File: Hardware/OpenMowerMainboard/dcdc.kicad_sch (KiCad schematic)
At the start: 24 parts, among them IC3 MAX20405AFOF_VY+T, U1 LM2596S_MODULE

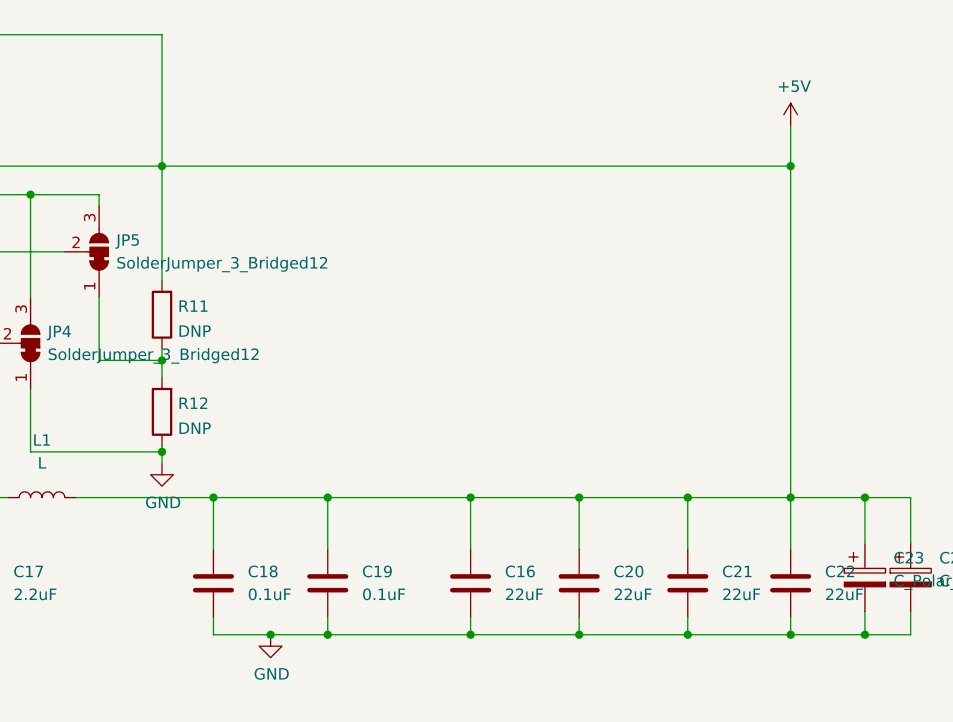
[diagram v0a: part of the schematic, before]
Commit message: v0_9_1 mainboard rework
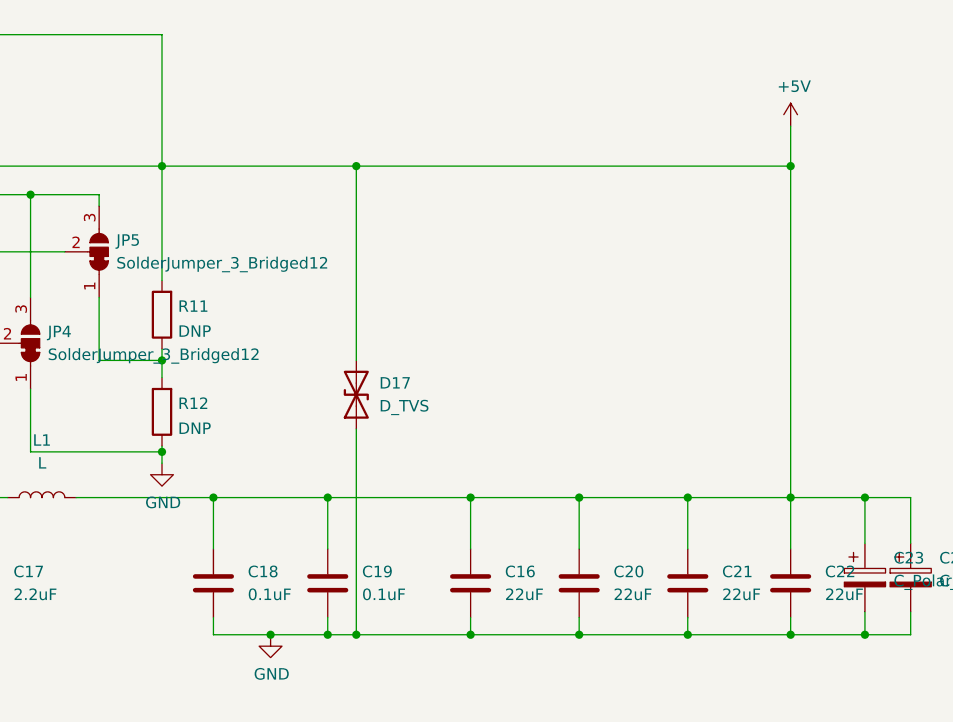
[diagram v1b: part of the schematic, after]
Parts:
- added D17: D_TVS, Diode_SMD:D_0402_1005Metric_Pad0.77x0.64mm_HandSolder, symbol Device:D_TVS
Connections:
- net +5V: now also D17.2 (A2)
- net GND: now also D17.1 (A1)
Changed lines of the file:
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@@
   (junction (at 93.345 109.855) (diameter 0) (color 0 0 0 0)
   )
+  (junction (at 186.69 90.17) (diameter 0) (color 0 0 0 0)
+  )
   (junction (at 223.52 142.24) (diameter 0) (color 0 0 0 0)
   )
@@
   )
   (junction (at 43.815 97.155) (diameter 0) (color 0 0 0 0)
+  )
+  (junction (at 186.69 142.24) (diameter 0) (color 0 0 0 0)
   )
   (junction (at 50.165 97.155) (diameter 0) (color 0 0 0 0)
@@
     (stroke (width 0) (type default) (color 0 0 0 0))
   )
+  (wire (pts (xy 186.69 90.17) (xy 186.69 111.76))
+    (stroke (width 0) (type default) (color 0 0 0 0))
+  )
   (wire (pts (xy 234.95 140.335) (xy 234.95 142.24))
     (stroke (width 0) (type default) (color 0 0 0 0))
@@
     (stroke (width 0) (type default) (color 0 0 0 0))
   )
-  (wire (pts (xy 165.1 90.17) (xy 234.95 90.17))
+  (wire (pts (xy 165.1 90.17) (xy 186.69 90.17))
     (stroke (width 0) (type default) (color 0 0 0 0))
   )
@@
     (stroke (width 0) (type default) (color 0 0 0 0))
   )
+  (wire (pts (xy 186.69 90.17) (xy 234.95 90.17))
+    (stroke (width 0) (type default) (color 0 0 0 0))
+  )
   (wire (pts (xy 234.95 127) (xy 243.205 127))
     (stroke (width 0) (type default) (color 0 0 0 0))
@@
     (stroke (width 0) (type default) (color 0 0 0 0))
   )
+  (wire (pts (xy 87.63 114.935) (xy 96.52 114.935))
+    (stroke (width 0) (type default) (color 0 0 0 0))
+  )
+  (wire (pts (xy 199.39 142.24) (xy 186.69 142.24))
+    (stroke (width 0) (type default) (color 0 0 0 0))
+  )
+  (wire (pts (xy 199.39 140.335) (xy 199.39 142.24))
+    (stroke (width 0) (type default) (color 0 0 0 0))
+  )
+  (wire (pts (xy 137.795 90.17) (xy 165.1 90.17))
+    (stroke (width 0) (type default) (color 0 0 0 0))
+  )
+  (wire (pts (xy 134.62 120.015) (xy 139.065 120.015))
+    (stroke (width 0) (type default) (color 0 0 0 0))
+  )
+  (wire (pts (xy 243.205 127) (xy 248.285 127))
+    (stroke (width 0) (type default) (color 0 0 0 0))
+  )
+  (wire (pts (xy 33.655 97.155) (xy 43.815 97.155))
+    (stroke (width 0) (type default) (color 0 0 0 0))
+  )
   (wire (pts (xy 199.39 127) (xy 211.455 127))
     (stroke (width 0) (type default) (color 0 0 0 0))
   )
-  (wire (pts (xy 87.63 114.935) (xy 96.52 114.935))
-    (stroke (width 0) (type default) (color 0 0 0 0))
-  )
-  (wire (pts (xy 199.39 142.24) (xy 183.515 142.24))
-    (stroke (width 0) (type default) (color 0 0 0 0))
-  )
-  (wire (pts (xy 199.39 140.335) (xy 199.39 142.24))
-    (stroke (width 0) (type default) (color 0 0 0 0))
-  )
-  (wire (pts (xy 137.795 90.17) (xy 165.1 90.17))
-    (stroke (width 0) (type default) (color 0 0 0 0))
-  )
-  (wire (pts (xy 134.62 120.015) (xy 139.065 120.015))
-    (stroke (width 0) (type default) (color 0 0 0 0))
-  )
-  (wire (pts (xy 243.205 127) (xy 248.285 127))
-    (stroke (width 0) (type default) (color 0 0 0 0))
-  )
-  (wire (pts (xy 33.655 97.155) (xy 43.815 97.155))
-    (stroke (width 0) (type default) (color 0 0 0 0))
-  )
   (wire (pts (xy 243.205 139.7) (xy 243.205 142.24))
     (stroke (width 0) (type default) (color 0 0 0 0))
@@
     (stroke (width 0) (type default) (color 0 0 0 0))
   )
+  (wire (pts (xy 186.69 142.24) (xy 183.515 142.24))
+    (stroke (width 0) (type default) (color 0 0 0 0))
+  )
   (wire (pts (xy 199.39 127) (xy 199.39 132.715))
     (stroke (width 0) (type default) (color 0 0 0 0))
@@
   )
   (wire (pts (xy 150.495 93.345) (xy 158.115 93.345))
+    (stroke (width 0) (type default) (color 0 0 0 0))
+  )
+  (wire (pts (xy 186.69 119.38) (xy 186.69 142.24))
     (stroke (width 0) (type default) (color 0 0 0 0))
   )
@@
     (pin "1")
   )
+  (symbol (lib_id "Device:D_TVS") (at 186.69 115.57 90) (unit 1)
+    (in_bom yes) (on_board yes) (fields_autoplaced)
+    (property "Reference" "D17" (id 0) (at 189.23 114.2999 90)
+      (effects (font (size 1.27 1.27)) (justify right))
+    )
+    (property "Value" "D_TVS" (id 1) (at 189.23 116.8399 90)
+      (effects (font (size 1.27 1.27)) (justify right))
+    )
+    (property "Footprint" "Diode_SMD:D_0402_1005Metric_Pad0.77x0.64mm_HandSolder" (id 2) (at 186.69 115.57 0)
+      (effects (font (size 1.27 1.27)) hide)
+    )
+    (property "Datasheet" "~" (id 3) (at 186.69 115.57 0)
+      (effects (font (size 1.27 1.27)) hide)
+    )
+    (pin "1")
+    (pin "2")
+  )
   (symbol (lib_id "Device:C") (at 223.52 136.525 0) (unit 1)

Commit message: added some valued, exported iBOM
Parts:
- C10, C24: value C_Polarized -> 680uF
- C23, C9: value C_Polarized -> DNP
- D17: value D_TVS -> DNP
- L1: value L -> 4.7uH 5A
- R11: value DNP -> 53.6 1%
- R12: value DNP -> 10k 1%
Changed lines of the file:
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@@
       (effects (font (size 1.27 1.27)) (justify right))
     )
-    (property "Value" "DNP" (id 1) (at 166.878 119.3416 0)
+    (property "Value" "10k 1%" (id 1) (at 166.878 119.3416 0)
       (effects (font (size 1.27 1.27)) (justify right))
     )
@@
       (effects (font (size 1.27 1.27)) (justify left))
     )
-    (property "Value" "C_Polarized" (id 1) (at 31.75 106.4259 0)
+    (property "Value" "DNP" (id 1) (at 31.75 106.4259 0)
       (effects (font (size 1.27 1.27)) (justify left))
     )
@@
       (effects (font (size 1.27 1.27)) (justify left))
     )
-    (property "Value" "C_Polarized" (id 1) (at 36.83 106.4259 0)
+    (property "Value" "680uF" (id 1) (at 36.83 106.4259 0)
       (effects (font (size 1.27 1.27)) (justify left))
     )
@@
     (in_bom yes) (on_board yes) (fields_autoplaced)
     (property "Reference" "L1" (id 0) (at 151.765 120.65 90))
-    (property "Value" "L" (id 1) (at 151.765 123.19 90))
+    (property "Value" "4.7uH 5A" (id 1) (at 151.765 123.19 90))
     (property "Footprint" "Inductor_SMD:L_Vishay_IHLP-2525" (id 2) (at 151.765 127 0)
       (effects (font (size 1.27 1.27)) hide)
@@
       (effects (font (size 1.27 1.27)) (justify left))
     )
-    (property "Value" "C_Polarized" (id 1) (at 246.38 136.2709 0)
+    (property "Value" "DNP" (id 1) (at 246.38 136.2709 0)
       (effects (font (size 1.27 1.27)) (justify left))
     )
@@
       (effects (font (size 1.27 1.27)) (justify right))
     )
-    (property "Value" "D_TVS" (id 1) (at 189.23 116.8399 90)
+    (property "Value" "DNP" (id 1) (at 189.23 116.8399 90)
       (effects (font (size 1.27 1.27)) (justify right))
     )
@@
       (effects (font (size 1.27 1.27)) (justify right))
     )
-    (property "Value" "DNP" (id 1) (at 166.878 108.5466 0)
+    (property "Value" "53.6 1%" (id 1) (at 166.878 108.5466 0)
       (effects (font (size 1.27 1.27)) (justify right))
     )
@@
       (effects (font (size 1.27 1.27)) (justify left))
     )
-    (property "Value" "C_Polarized" (id 1) (at 251.46 136.2709 0)
-      (effects (font (size 1.27 1.27)) (justify left))
-    )
+    (property "Value" "680uF" (id 1) (at 251.46 136.2709 0)
+      (effects (font (size 1.27 1.27)) (justify left))
+    )

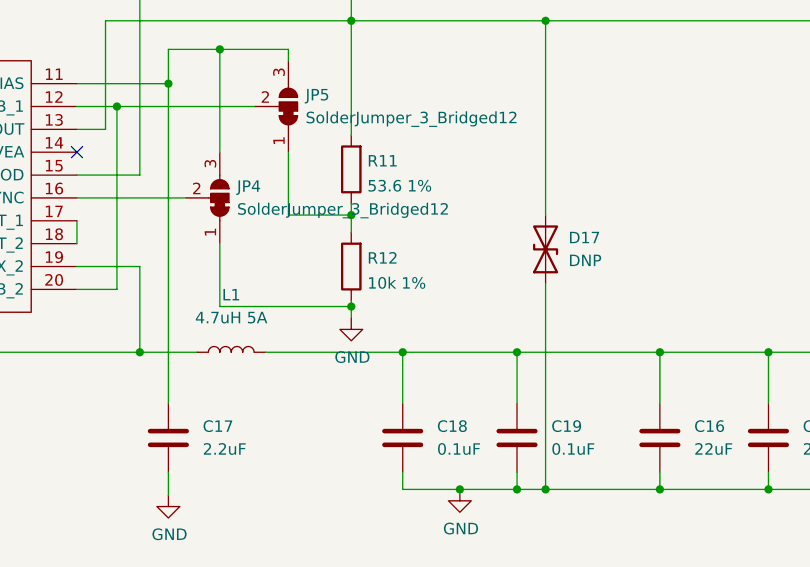
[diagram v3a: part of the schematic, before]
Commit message: BoM data added to kicad - results exported to .xlsx file
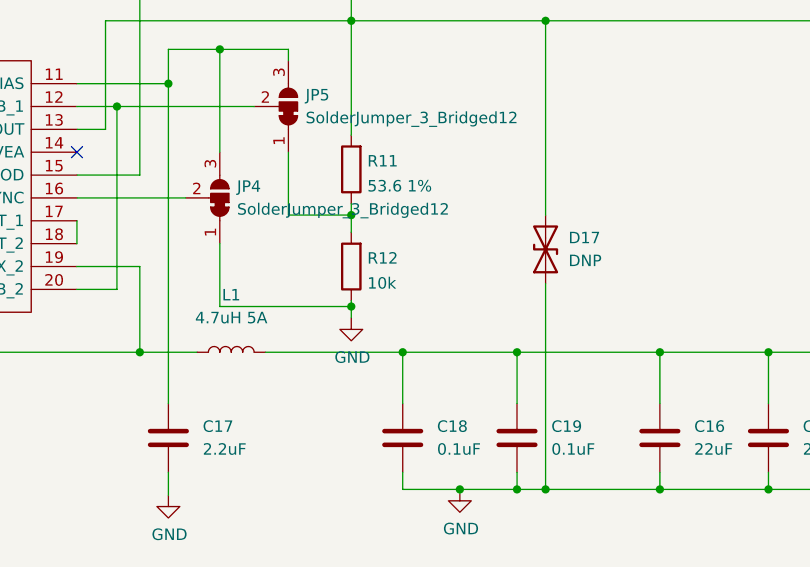
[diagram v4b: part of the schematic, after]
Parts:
- C10, C24: LCSC (none) -> C882153; Part Number (none) -> VEJ681M1VTR-1013; Stock_PN (none) -> CP-SMD-680uF-35V
- C11, C12: Digikey (none) -> 1276-3179-1-ND; Part Number (none) -> CL31B475KBHNFNE; Stock_PN (none) -> C-1206-4.7uF-50V-X7R
- C13, C14: Digikey (none) -> 1276-1029-1-ND; Part Number (none) -> CL21B105KBFNNNE; Stock_PN (none) -> C-805-1uF-50V-X7R
- C15, C18, C19: Digikey (none) -> 490-1331-1-ND; Part Number (none) -> CL10B104KC8NNNC; Stock_PN (none) -> C-603-.1uF-100V-X7R
- C16, C20, C21, C22: Digikey (none) -> 1276-3148-1-ND; Part Number (none) -> CL31B226MPHNNNE; Stock_PN (none) -> C-1206-22uF-10V-X7R
- C17: Digikey (none) -> 1276-1183-1-ND; Part Number (none) -> CL10A225KQ8NNNC; Stock_PN (none) -> C-603-2.2uF-6.3V-X5R
- C23, C9, D17, JP4, JP5, R8: Config (none) -> do not place
- IC3: Digikey (none) -> 175-MAX20405AFOD/VY+-ND; Part Number (none) -> MAX20405AFOD/VY+; Stock_PN (none) -> U-MAX20405
- L1: Digikey (none) -> 732-3354-1-ND; Part Number (none) -> 74437349047; Stock_PN (none) -> L-2525-47uH-5A
- R11: Digikey (none) -> RMCF0805FT53K6CT-ND; Part Number (none) -> RMCF0805FT53K6; Stock_PN (none) -> R-805-53.6K-.125W-1%
- R12: value 10k 1% -> 10k; Digikey (none) -> 738-RMCF0805FG10K0CT-ND; Part Number (none) -> RMCF0805FG10K0; Stock_PN (none) -> R-805-10K-.125W-1%
- U1: Config (none) -> bench_test; Digikey (none) -> LM2596SX-5.0/NOPBCT-ND; Part Number (none) -> LM2596SX-5.0/NOPB; Stock_PN (none) -> U-LM2596SX-5.0
